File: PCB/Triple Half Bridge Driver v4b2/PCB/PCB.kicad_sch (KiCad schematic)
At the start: 364 parts, among them J1 Screw_Terminal_01x06, J10 Screw_Terminal_01x02, J100 Screw_Terminal_01x02, J101 Screw_Terminal_01x02, J102 Screw_Terminal_01x02, J103 Screw_Terminal_01x02, J11 Screw_Terminal_01x02, J12 Screw_Terminal_01x02, J13 Screw_Terminal_01x03, J14 Screw_Terminal_01x03, J15 Screw_Terminal_01x03, J16 Screw_Terminal_01x03, J17 Screw_Terminal_01x02, J18 Screw_Terminal_01x02, J19 Screw_Terminal_01x02, J2 Screw_Terminal_01x03, J20 Screw_Terminal_01x02, J21 Screw_Terminal_01x03, J23 Screw_Terminal_01x01, J24 Screw_Terminal_01x03, J25 Screw_Terminal_01x03, J26 Screw_Terminal_01x02, J27 Screw_Terminal_01x02, J28 Screw_Terminal_01x01, J29 Screw_Terminal_01x02, J3 Screw_Terminal_01x03, J30 Screw_Terminal_01x02, J31 Screw_Terminal_01x02, J32 Screw_Terminal_01x02, J33 Screw_Terminal_01x02, J34 Screw_Terminal_01x02, J35 Screw_Terminal_01x02, J36 Screw_Terminal_01x02, J37 Screw_Terminal_01x02, J38 Screw_Terminal_01x02, J39 Screw_Terminal_01x02, J4 Screw_Terminal_01x03, J40 Screw_Terminal_01x02, J41 Screw_Terminal_01x02, J42 Screw_Terminal_01x02, J43 Screw_Terminal_01x02, J44 Screw_Terminal_01x01, J45 Screw_Terminal_01x02, J46 Screw_Terminal_01x02, J47 Screw_Terminal_01x02, J48 Screw_Terminal_01x02, J49 Screw_Terminal_01x02, J5 Screw_Terminal_01x03, J50 Screw_Terminal_01x02, J51 Screw_Terminal_01x02, J52 Screw_Terminal_01x02, J53 Screw_Terminal_01x02, J54 Screw_Terminal_01x02, J55 Screw_Terminal_01x02, J56 Screw_Terminal_01x02, J57 Screw_Terminal_01x02, J58 Screw_Terminal_01x02, J59 Screw_Terminal_01x02, J6 Screw_Terminal_01x02, J60 Screw_Terminal_01x02, J61 Screw_Terminal_01x02, J62 Screw_Terminal_01x02, J63 Screw_Terminal_01x02, J64 Screw_Terminal_01x02, J65 Screw_Terminal_01x02, J66 Screw_Terminal_01x02, J67 Screw_Terminal_01x02, J68 Screw_Terminal_01x02, J69 Screw_Terminal_01x02, J7 Screw_Terminal_01x06, J70 Screw_Terminal_01x02, J71 Screw_Terminal_01x02, J72 Screw_Terminal_01x02, J73 Screw_Terminal_01x02, J74 Screw_Terminal_01x02, J75 Screw_Terminal_01x02, J76 Screw_Terminal_01x02, J77 Screw_Terminal_01x02, J78 Screw_Terminal_01x02, J79 Screw_Terminal_01x02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

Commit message: Remove unused gerber files
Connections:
- net GND: now also FB3.1
- net GND1: no longer FB3.1
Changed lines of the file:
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@@
 	(wire
 		(pts
-			(xy 548.64 107.95) (xy 548.64 114.3)
+			(xy 548.64 105.41) (xy 548.64 114.3)
 		)
 		(stroke
@@
 	)
 	(symbol
+		(lib_id "power:GND")
+		(at 548.64 105.41 180)
+		(unit 1)
+		(exclude_from_sim no)
+		(in_bom yes)
+		(on_board yes)
+		(dnp no)
+		(fields_autoplaced yes)
+		(property "Reference" "#PWR0158"
+			(at 548.64 99.06 0)
+			(effects
+				(font
+					(size 1.27 1.27)
+				)
+				(hide yes)
+			)
+		)
+		(property "Value" "GND"
+			(at 548.64 100.33 0)
+			(effects
+				(font
+					(size 1.27 1.27)
+				)
+			)
+		)
+		(property "Footprint" ""
+			(at 548.64 105.41 0)
+			(effects
+				(font
+					(size 1.27 1.27)
+				)
+				(hide yes)
+			)
+		)
+		(property "Datasheet" ""
+			(at 548.64 105.41 0)
+			(effects
+				(font
+					(size 1.27 1.27)
+				)
+				(hide yes)
+			)
+		)
+		(property "Description" "Power symbol creates a global label with name \"GND\" , ground"
+			(at 548.64 105.41 0)
+			(effects
+				(font
+					(size 1.27 1.27)
+				)
+				(hide yes)
+			)
+		)
+		(pin "1"
+		)
+		(instances
+			(project ""
+				(path "/e63e39d7-6ac0-4ffd-8aa3-1841a4541b55"
+					(reference "#PWR0158")
+					(unit 1)
+				)
+			)
+		)
+	)
+	(symbol
 		(lib_id "Driver_FET:IRS2101")
 		(at 82.55 505.46 0)
@@
 					(unit 1)
 				)
-			)
-		)
-	)
-	(symbol
-		(lib_id "power:GND1")
-		(at 548.64 107.95 180)
-		(unit 1)
-		(exclude_from_sim no)
-		(in_bom yes)
-		(on_board yes)
-		(dnp no)
-		(fields_autoplaced yes)
-		(property "Reference" "#PWR0158"
-			(at 548.64 101.6 0)
-			(effects
-				(font
-					(size 1.27 1.27)
-				)
-				(hide yes)
-			)
-		)
-		(property "Value" "GND1"
-			(at 548.64 102.87 0)
-			(effects
-				(font
-					(size 1.27 1.27)
-				)
-			)
-		)
-		(property "Footprint" ""
-			(at 548.64 107.95 0)
-			(effects
-				(font
-					(size 1.27 1.27)
-				)
-				(hide yes)
-			)
-		)
-		(property "Datasheet" ""
-			(at 548.64 107.95 0)
-			(effects
-				(font
-					(size 1.27 1.27)
-				)
-				(hide yes)
-			)
-		)
-		(property "Description" "Power symbol creates a global label with name \"GND1\" , ground"
-			(at 548.64 107.95 0)
-			(effects
-				(font
-					(size 1.27 1.27)
-				)
-				(hide yes)
-			)
-		)
-		(pin "1"
-		)
-		(instances
-			(project ""
-				(path "/e63e39d7-6ac0-4ffd-8aa3-1841a4541b55"
-					(reference "#PWR0158")
-					(unit 1)
-				)

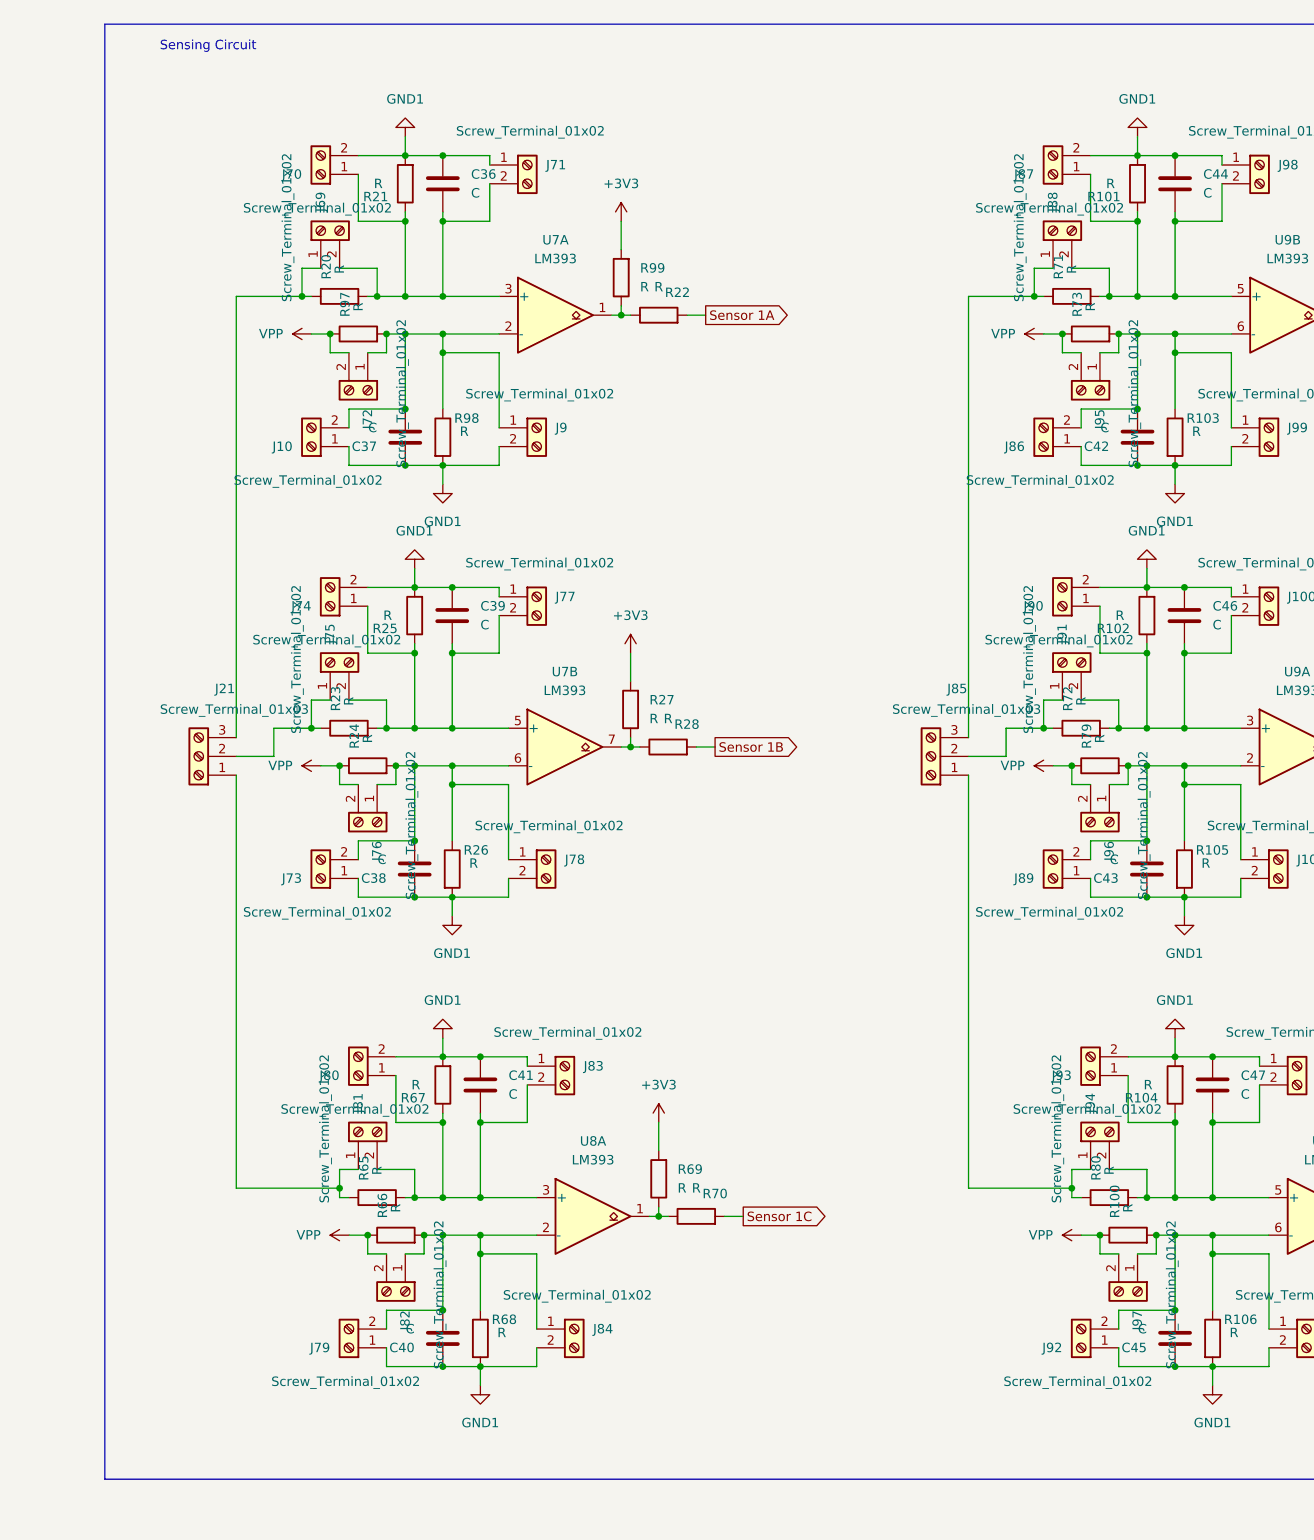
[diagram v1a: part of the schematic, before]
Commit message: Add datasheets for components used
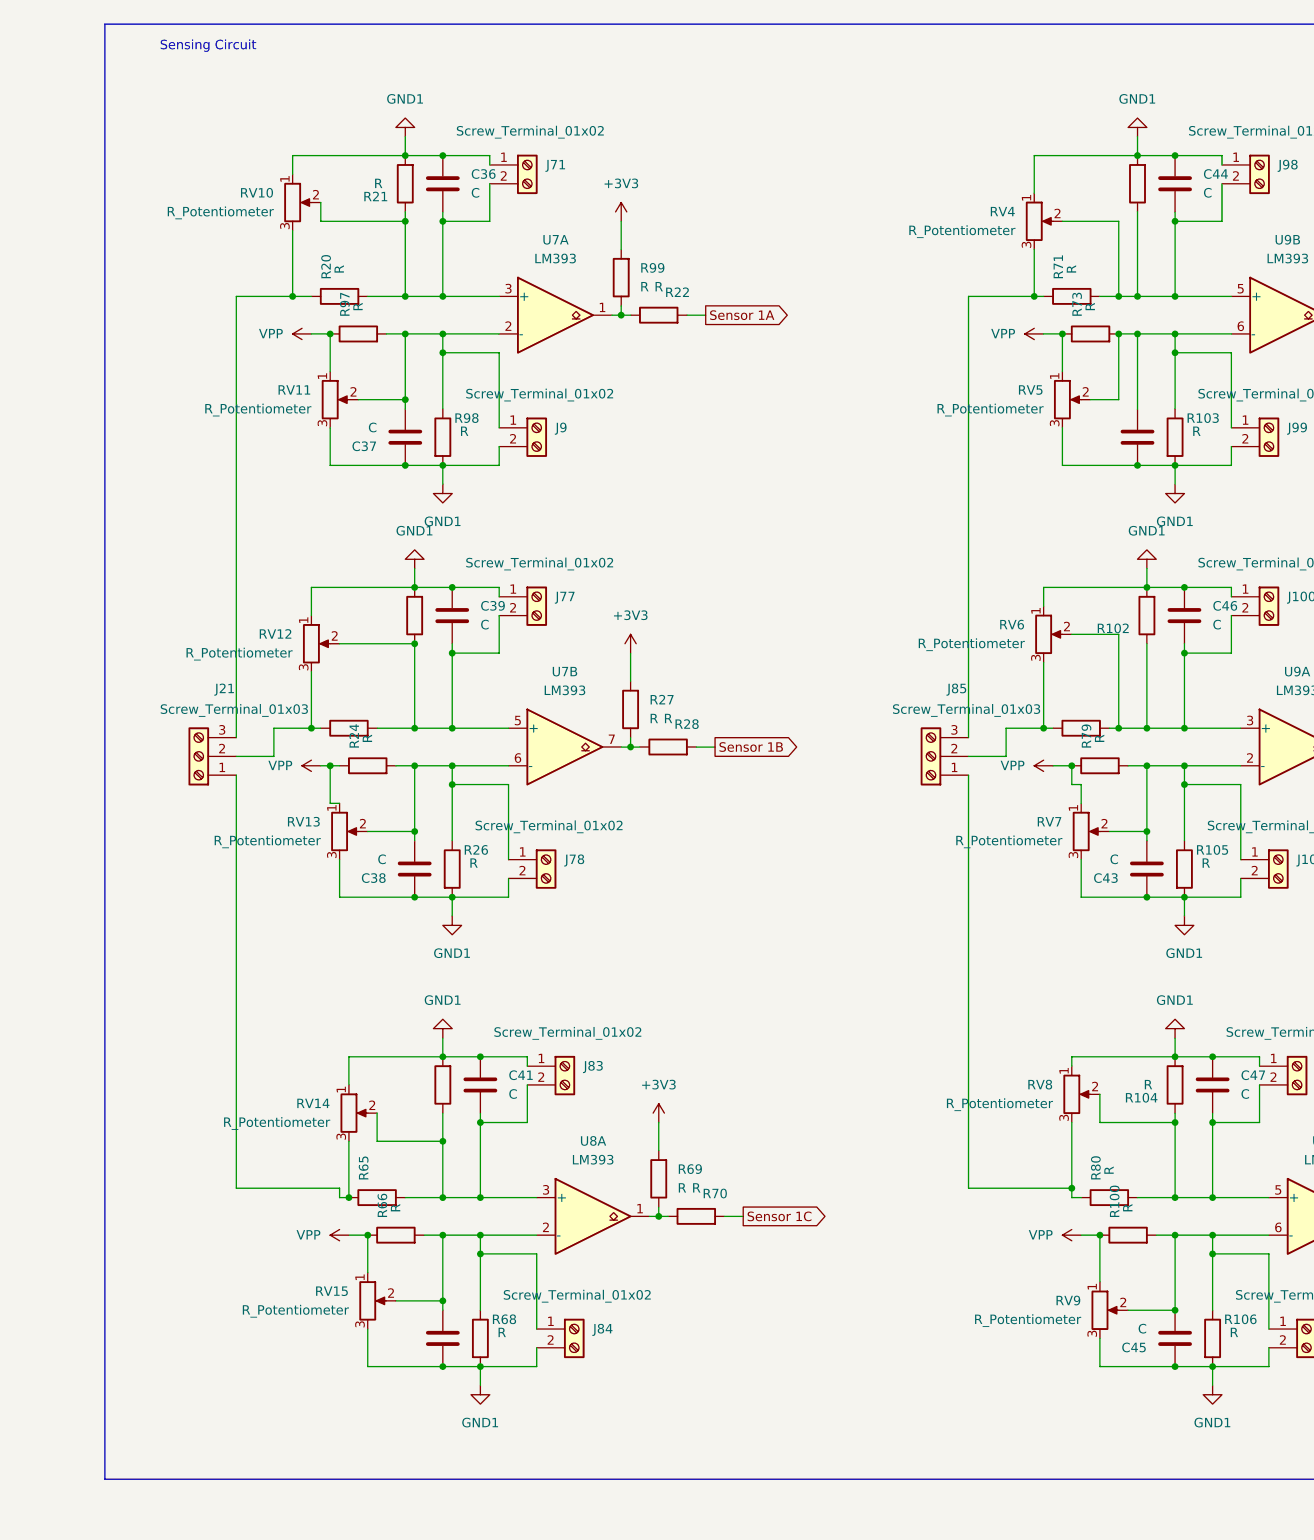
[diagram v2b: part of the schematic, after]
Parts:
- removed J10, J69, J70, J72, J73, J74, J75, J76, J79, J80, J81, J82, J86, J87, J88, J89, J90, J91, J92, J93, J94, J95, J96, J97: Screw_Terminal_01x02, 3 Pin Spring Terminal:1792863, symbol Connector:Screw_Terminal_01x02
- added RV10, RV11, RV12, RV13, RV14, RV15, RV4, RV5, RV6, RV7, RV8, RV9: R_Potentiometer, Potentiometer_THT:Potentiometer_Alps_RK09K_Single_Vertical, symbol Device:R_Potentiometer
- J100, J101, J102, J103, J45, J46, J47, J48, J49, J50, J51, J52, J53, J54, J55, J56, J57, J58, J59, J60, J61, J62, J63, J64, J65, J66, J67, J68, J71, J77, J78, J83, J84, J98, J99: footprint 3 Pin Spring Terminal:1792863 -> TerminalBlock_4Ucon:TerminalBlock_4Ucon_1x02_P3.50mm_Horizontal
- J27, J29, J30, J31, J32, J33, J34, J35, J36, J37, J38, J39, J40, J41, J42, J43: footprint Connector_PinSocket_2.54mm:PinSocket_1x02_P2.54mm_Vertical -> TerminalBlock_4Ucon:TerminalBlock_4Ucon_1x02_P3.50mm_Horizontal
- J28: footprint Connector_PinHeader_2.54mm:PinHeader_1x01_P2.54mm_Vertical -> TerminalBlock_4Ucon:TerminalBlock_4Ucon_1x02_P3.50mm_Horizontal
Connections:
- net GND1: now also RV10.1, RV11.3, RV12.1, RV13.3, RV14.1, RV15.3, RV4.1, RV5.3, RV6.1, RV7.3, RV8.1, RV9.3
- net VPP: now also RV11.1, RV13.1, RV15.1, RV5.1, RV7.1, RV9.1
- net at C41.2, J83.2 (Pin_2), R65.2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: now also RV14.2
- net at C39.2, J77.2 (Pin_2), R23.2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: now also RV12.2
- net at C38.2, J78.1 (Pin_1), R24.2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: now also RV13.2
- net at C45.2, J103.1 (Pin_1), R100.2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: now also RV9.2
- net at C37.2, J9.1 (Pin_1), R97.2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: now also RV11.2
- net at J21.1 (Pin_1), R65.1: now also RV14.3
- net at J21.2 (Pin_2), R23.1: now also RV12.3
- net at J21.3 (Pin_3), R20.1: now also RV10.3
- net at C44.2, J98.2 (Pin_2), R101.1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: now also RV4.2
- net at C36.2, J71.2 (Pin_2), R20.2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: now also RV10.2
- net at C42.2, J99.1 (Pin_1), R103.1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: now also RV5.2
- net at C47.2, J102.2 (Pin_2), R104.1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: now also RV8.2
- net at J85.3 (Pin_3), R71.1: now also RV4.3
- net at C46.2, J100.2 (Pin_2), R102.1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: now also RV6.2
- net at J85.1 (Pin_1), R80.1: now also RV8.3
- net at J85.2 (Pin_2), R72.1: now also RV6.3
- net at C40.2, J84.1 (Pin_1), R66.2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: now also RV15.2
- net at C43.2, J101.1 (Pin_1), R105.1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: now also RV7.2
